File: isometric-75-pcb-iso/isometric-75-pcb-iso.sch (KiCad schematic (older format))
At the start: 10 parts

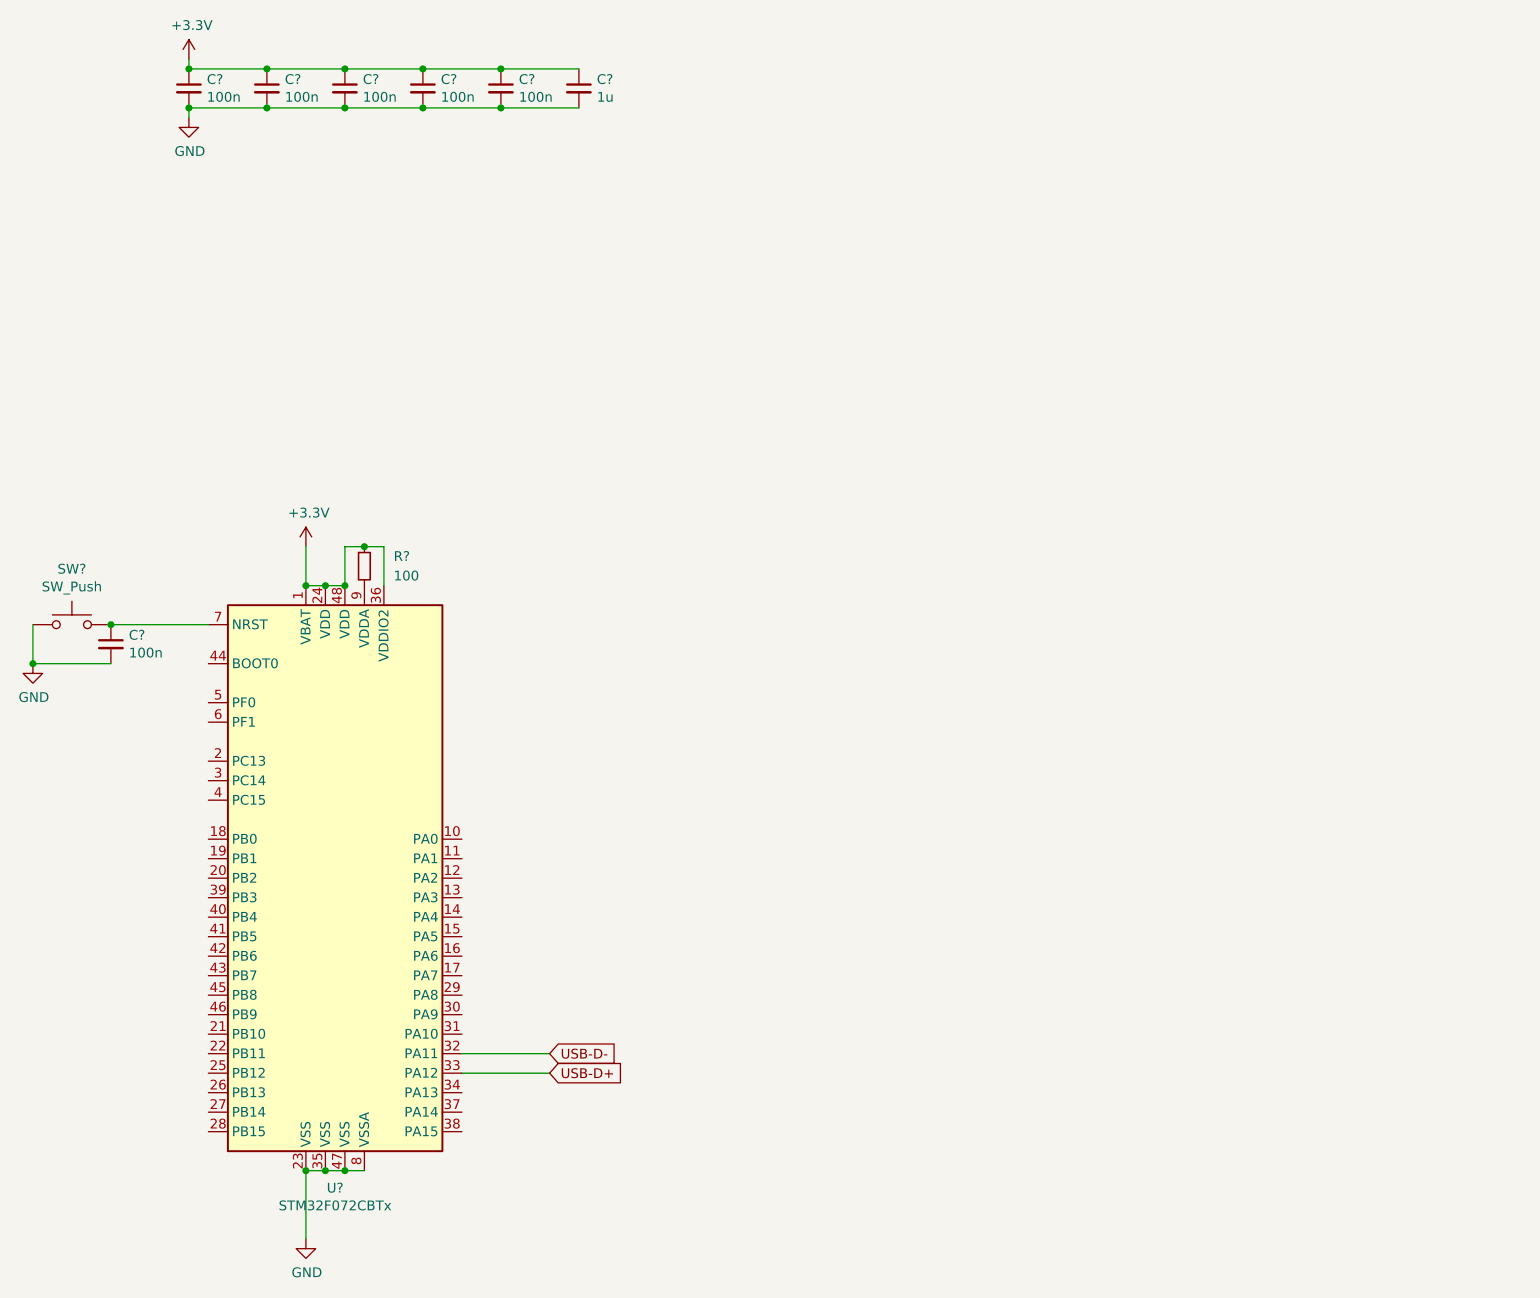
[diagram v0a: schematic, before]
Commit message: added key matrix
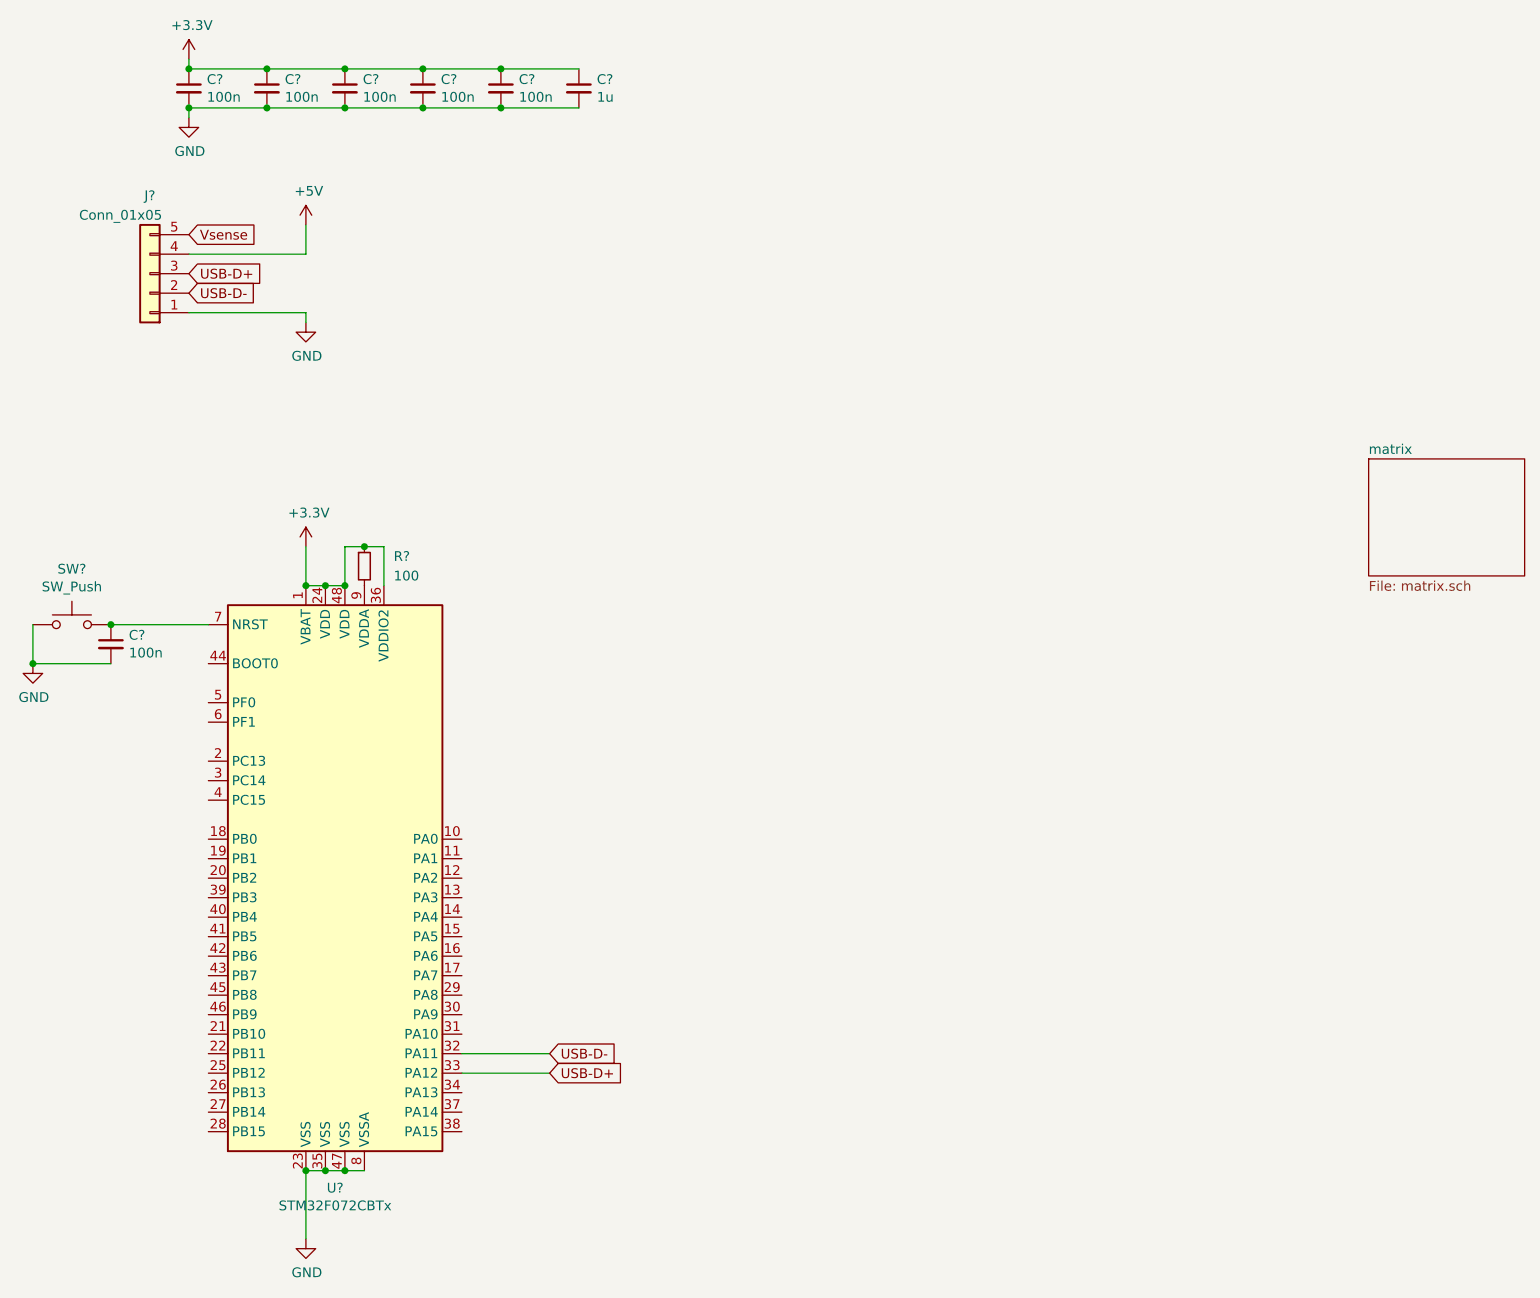
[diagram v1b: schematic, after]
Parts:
- added J?: Conn_01x05, Connector_JST:JST_PH_S5B-PH-SM4-TB_1x05-1MP_P2.00mm_Horizontal, symbol Connector_Generic:Conn_01x05
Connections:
- net GND: now also J?.1 (Pin_1)
- net USB-D+: now also J?.3 (Pin_3)
- net USB-D-: now also J?.2 (Pin_2)
- new net +5V: J?.4 (Pin_4)
- new net Vsense: J?.5 (Pin_5)
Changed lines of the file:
@@
 $Descr A4 11693 8268
 encoding utf-8
-Sheet 1 1
+Sheet 1 2
 Title ""
 Date ""
@@
 Wire Wire Line
 	1100 3850 1600 3850
+$Comp
+L Connector_Generic:Conn_01x05 J?
+U 1 1 5E640E55
+P 1300 2050
+F 0 "J?" H 1300 1650 50  0000 C CNN
+F 1 "Conn_01x05" H 1450 1750 50  0000 C CNN
+F 2 "Connector_JST:JST_PH_S5B-PH-SM4-TB_1x05-1MP_P2.00mm_Horizontal" H 1300 2050 50  0001 C CNN
+F 3 "http://www.jst-mfg.com/product/pdf/eng/ePH.pdf" H 1300 2050 50  0001 C CNN
+	1    1300 2050
+	-1   0    0    1
+$EndComp
+$Comp
+L power:GND #PWR?
+U 1 1 5E644973
+P 2100 2300
+F 0 "#PWR?" H 2100 2050 50  0001 C CNN
+F 1 "GND" H 2105 2127 50  0000 C CNN
+F 2 "" H 2100 2300 50  0001 C CNN
+F 3 "" H 2100 2300 50  0001 C CNN
+	1    2100 2300
+	1    0    0    -1
+$EndComp
+$Comp
+L power:+5V #PWR?
+U 1 1 5E645E1A
+P 2100 1800
+F 0 "#PWR?" H 2100 1650 50  0001 C CNN
+F 1 "+5V" H 2115 1973 50  0000 C CNN
+F 2 "" H 2100 1800 50  0001 C CNN
+F 3 "" H 2100 1800 50  0001 C CNN
+	1    2100 1800
+	1    0    0    -1
+$EndComp
+Text GLabel 1500 2150 2    50   Input ~ 0
+USB-D-
+Text GLabel 1500 2050 2    50   Input ~ 0
+USB-D+
+Text GLabel 1500 1850 2    50   Input ~ 0
+Vsense
+Wire Wire Line
+	2100 1950 2100 1800
+Wire Wire Line
+	1500 1950 2100 1950
+Wire Wire Line
+	2100 2250 2100 2300
+Wire Wire Line
+	1500 2250 2100 2250
+$Sheet
+S 7550 3000 800  600
+U 5E64D9E7
+F0 "matrix" 50
+F1 "matrix.sch" 50
+$EndSheet
 $EndSCHEMATC
